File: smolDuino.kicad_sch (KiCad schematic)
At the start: 52 parts, among them J1 Barrel_Jack_Switch, J2 USB_C_Receptacle_USB2.0, J3 2x3 SPI Header, J4 2x5 HV Outputs, J5 I^{2}C Connector, P1 CONN_01X01, P2 CONN_01X01, P3 CONN_01X01, P4 CONN_01X01, P5 Digital, P6 Power, P7 Digital, P8 Analog, Q1 AO3401A, SW1 Enable, SW2 Reset, U1 AP62250smol_A, U2 rp2040smol-c-unit, U3 74AHCT1G04, U4 Charj_smol, U5 AT24CS02-STUM, U6 SN74AHCT125N

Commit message: commit before I ruin too much
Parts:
- added C?: 1uF, Capacitor_SMD:C_0603_1608Metric, symbol Device:C
- added C? (x2): 10uF, Capacitor_SMD:C_0603_1608Metric, symbol Device:C
- added D?: UPS120, MikeFootprintLib:UPS120_D_Powermite_AK, symbol MikeLib:UPS120
- added Q?: AO3401A, Package_TO_SOT_SMD:SOT-23, symbol Transistor_FET:AO3401A
- added R?: 100K, Resistor_SMD:R_0402_1005Metric, symbol Device:R
- added R?: 4.7k, Resistor_SMD:R_0603_1608Metric_Pad0.98x0.95mm_HandSolder, symbol Device:R
- added R?: 1k, Resistor_SMD:R_0402_1005Metric, symbol Device:R
- added U?: LC709203FXE-05MH, MikeFootprintLib:WLCSP9-1.60x1.76mm, symbol MikeLib:LC709203FXE-05MH
- added U?: MCP73831-2-OT, Package_TO_SOT_SMD:SOT-23-5, symbol Battery_Management:MCP73831-2-OT
- P1, P2, P3, P4: now left out of the parts list
- U6: footprint Package_DFN_QFN:Texas_S-PVQFN-N14 -> MikeFootprintLib:74x125_Texas_S-PVQFN-N14
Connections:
- net GND: now also C?.2, C?.2, C?.2, R?.1, U?.2 (VSS), U?.A1 (VSS), U?.B1 (TEST)
- new net: R?.1, U?.1 (STAT)
- new net: R?.2, U?.5 (PROG)
- new net +BATT: C?.1, C?.1, Q?.3 (D), U?.3 (VBAT), U?.A3 (VDD)
- new net SCL: U?.C2 (SCL)
- new net V_{High}Out: D?.1 (K), Q?.2 (S)
- new net V_{USB_Charge}: C?.1, U?.4 (VDD)
- new net V_{USB}: D?.2 (A), Q?.1 (G), R?.2
- new net ~{ChargeEnable}: R?.1
- new net ~{STAT}: R?.2
- no-connect marks 15 -> 18
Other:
- note added: "Charger"
- note added: "Gas Gauge"
- note added: "R2 can be fit with 0 Ohm resistor to allow external charge rate selection"
- note added: "USB -> Battery Backfeed Protection"
- note added: "V_{High} -> 5V if USB connected, else V_{Batt}"

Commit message: Removed the extra stuff i added
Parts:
- removed C?: 1uF, Capacitor_SMD:C_0603_1608Metric, symbol Device:C
- removed C? (x2): 10uF, Capacitor_SMD:C_0603_1608Metric, symbol Device:C
- removed D?: UPS120, MikeFootprintLib:UPS120_D_Powermite_AK, symbol MikeLib:UPS120
- removed Q?: AO3401A, Package_TO_SOT_SMD:SOT-23, symbol Transistor_FET:AO3401A
- removed R?: 100K, Resistor_SMD:R_0402_1005Metric, symbol Device:R
- removed R?: 4.7k, Resistor_SMD:R_0603_1608Metric_Pad0.98x0.95mm_HandSolder, symbol Device:R
- removed R?: 1k, Resistor_SMD:R_0402_1005Metric, symbol Device:R
- removed U?: LC709203FXE-05MH, MikeFootprintLib:WLCSP9-1.60x1.76mm, symbol MikeLib:LC709203FXE-05MH
- removed U?: MCP73831-2-OT, Package_TO_SOT_SMD:SOT-23-5, symbol Battery_Management:MCP73831-2-OT
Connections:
- no-connect marks 18 -> 15
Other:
- note removed: "Charger"
- note removed: "Gas Gauge"
- note removed: "R2 can be fit with 0 Ohm resistor to allow external charge rate selection"
- note removed: "USB -> Battery Backfeed Protection"
- note removed: "V_{High} -> 5V if USB connected, else V_{Batt}"

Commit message: Progress
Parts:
- added C1: 47u, Capacitor_SMD:CP_Elec_6.3x5.4, symbol Device:C_Polarized
- added D3: ChargeEn, LED_SMD:LED_0603_1608Metric, symbol Device:LED
- added R8: 2k, Resistor_SMD:R_0603_1608Metric, symbol Device:R
- C2: renamed from C1; value 10uF -> 4u7
- C3: renamed from C2; value 100nF -> 100n
- C4, C5: value 100nF -> 100n
- J1: value Barrel_Jack_Switch -> DC Barrel Jack
- U1: value AP62250smol_A -> AP62250smol; footprint MikePCBAs:AP62250smol_A -> MikePCBAs:AP62250smol_C
- renumbered ART3 to ART2, ART4 to ART3, ART2 to ART4, C3 to C6, D3 to D4, JP2 to JP1, JP3 to JP2, JP1 to JP3, R6 to R5, R7 to R6, R5 to R7, U6 to U3, U5 to U4, U3 to U5, U4 to U6
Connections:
- net GND: now also C1.2
- net VCC: now also R8.1
- net VIN: now also C1.1
- net ~{ChargeEn}: now reaches U5.4, U6.5 (~{ChargeEnable})
- net ~{ChargeEn}: now also D3.1 (K)
- net STAT: now reaches D4.1 (K), U6.6 (~{STAT})
- net CC2: now reaches J2.B5 (CC2), R4.2
- net V_{Bus}: now reaches F2.1, J2.A4 (VBUS), J2.A9 (VBUS), J2.B4 (VBUS), J2.B9 (VBUS)
- net CC1: now reaches J2.A5 (CC1), R2.2
- net V_{Bus}_{Fused}: now reaches C2.2, C3.1, F2.2, Q1.3 (D)
- new net: D3.2 (A), R8.2
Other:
- moved on the sheet: C4, D4, F1, J1, JP3, U6

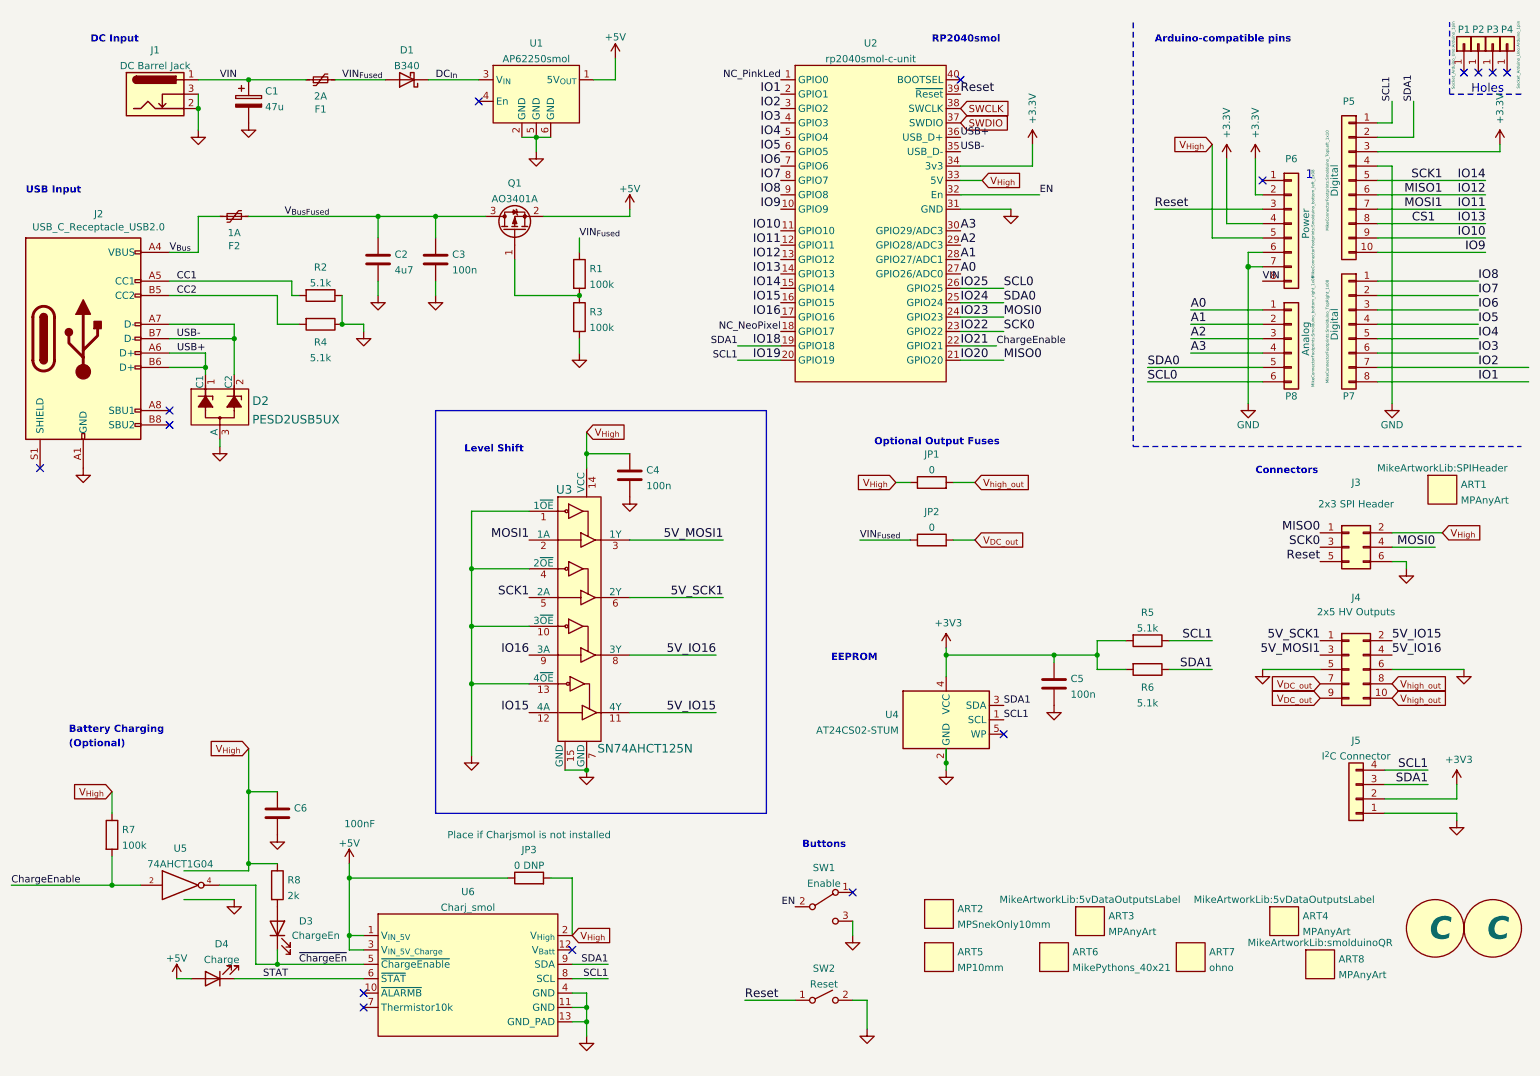
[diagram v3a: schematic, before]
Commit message: More progress. Charjsmol is removed and integrated directly onto the board.
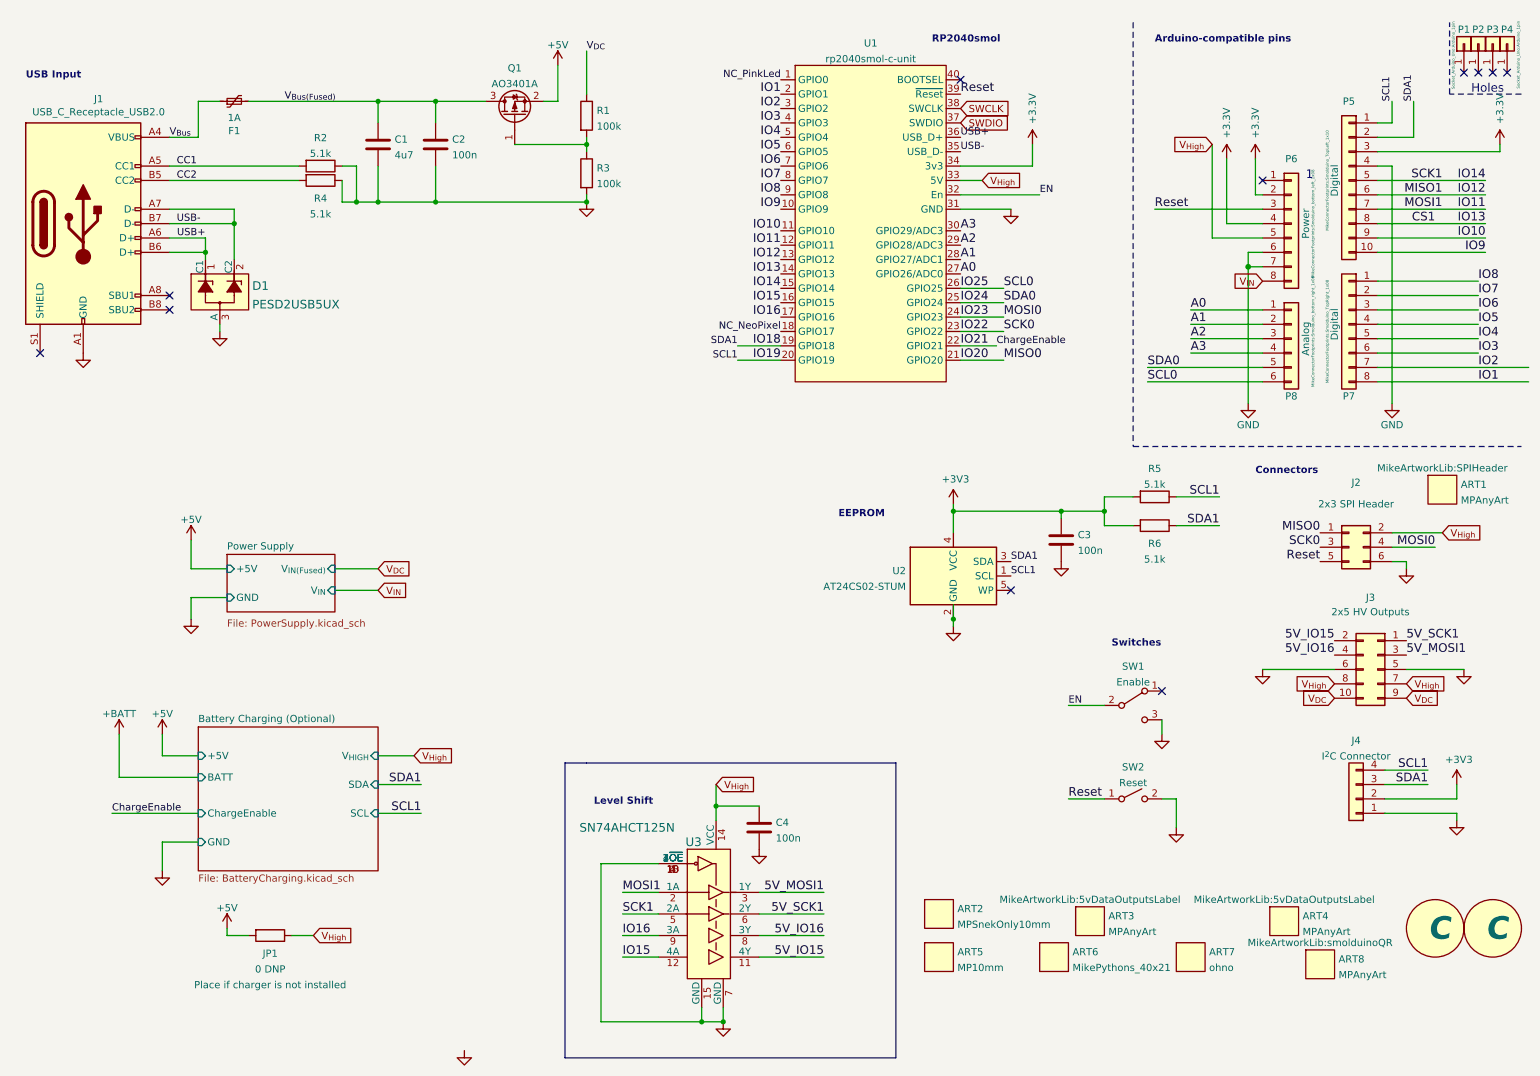
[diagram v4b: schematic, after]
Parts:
- removed C1: 47u, Capacitor_SMD:CP_Elec_6.3x5.4, symbol Device:C_Polarized
- removed C6: 100nF, Capacitor_SMD:C_0603_1608Metric, symbol Device:C
- removed D1: B340, Diode_SMD:D_SMC, symbol Diode:B340
- removed D3: ChargeEn, LED_SMD:LED_0603_1608Metric, symbol Device:LED
- removed D4: Charge, LED_SMD:LED_0603_1608Metric, symbol Device:LED
- removed F1: 2A, Fuse:Fuse_2920_7451Metric, symbol Device:Polyfuse_Small
- removed J1: DC Barrel Jack, Connector_BarrelJack:BarrelJack_GCT_DCJ200-10-A_Horizontal, symbol Connector:Barrel_Jack_Switch
- removed JP2: 0, MikeFootprintLib:R_0OHM_1206_3216Metric, symbol Device:R
- removed JP3: 0 DNP, MikeFootprintLib:R_0OHM_1206_3216Metric, symbol Device:R
- removed R7: 100k, Resistor_SMD:R_0603_1608Metric, symbol Device:R
- removed R8: 2k, Resistor_SMD:R_0603_1608Metric, symbol Device:R
- removed U1: AP62250smol, MikePCBAs:AP62250smol_C, symbol MikeLib:AP62250smol_A
- removed U5: 74AHCT1G04, Package_TO_SOT_SMD:SOT-353_SC-70-5, symbol 74xGxx:74AHCT1G04
- removed U6: Charj_smol, MikePCBAs:Charj_smol_B, symbol MikeLib:Charj_smol
- JP1: value 0 -> 0 DNP; Field4 (none) -> Place if charger is not installed
- U3: footprint MikeFootprintLib:74x125_Texas_S-PVQFN-N14 -> Package_DFN_QFN:Texas_S-PVQFN-N14; symbol MikeLib:SN74AHCT125N -> MikeLib:SN74AHCT125N_OETied
- renumbered C2 to C1, C3 to C2, C5 to C3, D2 to D1, F2 to F1, J2 to J1, J3 to J2, J4 to J3, J5 to J4, U2 to U1, U4 to U2
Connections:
- net +5V: now also JP1.2
- net VCC renamed V_{High}
- net V_{High}: now also J3.7 (Pin_7), J3.8 (Pin_8)
- net VIN renamed V_{IN}
- net VIN_{Fused} renamed V_{DC}
- net V_{DC}: now also J3.10 (Pin_10), J3.9 (Pin_9)
- net V_{Bus}_{Fused} renamed V_{Bus}_{(Fused)}
- removed net V_{DC_out}: J3.7 (Pin_7), J3.9 (Pin_9)
- removed net V_{high_out}: J3.10 (Pin_10), J3.8 (Pin_8), JP1.2
- no-connect marks 15 -> 11
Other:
- added sheet Battery Charging (Optional) (BatteryCharging.kicad_sch)
- added sheet Power Supply (PowerSupply.kicad_sch)
- note added: "Switches"
- note removed: "(Optional)"
- note removed: "Battery Charging"
- note removed: "Buttons"
- note removed: "DC Input"
- note removed: "Optional Output Fuses"
- moved on the sheet: C1, C2, C3, C4, D1, F1, J1, J3, Q1, R1, R2, R3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

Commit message: Rev C, I think
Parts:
- removed ART3, ART4: MPAnyArt, MikeArtworkLib:5vDataOutputsLabel, symbol MikeArtworkLib:MPAnyArt
- added JP1: Jumper_2_Bridged, Jumper:SolderJumper-2_P1.3mm_Bridged_Pad1.0x1.5mm, symbol Jumper:Jumper_2_Bridged
- J3: footprint MikeConnectorFootprints:smolduino_2x05_header -> MikeConnectorFootprints:PinSocket_2x06_P2.54mm_Vertical; symbol Connector_Generic:Conn_02x05_Odd_Even -> Connector_Generic:Conn_02x06_Odd_Even
- JP2: renamed from JP1; value 0 DNP -> Battery Protection Diode Bypass; footprint MikeFootprintLib:R_0OHM_1206_3216Metric -> Jumper:SolderJumper-2_P1.3mm_Open_TrianglePad1.0x1.5mm; symbol Device:R -> Jumper:SolderJumper_2_Open; now left out of the parts list
- renumbered ART5 to ART3, ART6 to ART4, ART7 to ART5, ART8 to ART6
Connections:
- net +5V: now also J3.10 (Pin_10), J3.9 (Pin_9), P6.5 (Pin_5)
- net EN: now also JP1.1 (A); no longer U1.32 (En)
- net V_{DC}: now also J3.11 (Pin_11), J3.12 (Pin_12); no longer J3.10 (Pin_10), J3.9 (Pin_9)
- net V_{High}: no longer P6.5 (Pin_5)
- new net EN_Pin: JP1.2 (B), U1.32 (En)

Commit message: Remove Gas Gauge IC
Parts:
- MISC1, MISC2: value C -> D
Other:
- sheet Battery Charging (Optional) ports: added none; removed SCL, SDA
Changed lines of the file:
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@@
-    (stroke (width 0) (type default) (color 0 0 0 0))
-  )
-  (wire (pts (xy 82.55 147.32) (xy 90.17 147.32))
     (stroke (width 0) (type default) (color 0 0 0 0))
   )
@@
     (stroke (width 0) (type default) (color 0 0 0 0))
   )
-  (wire (pts (xy 82.55 152.4) (xy 90.17 152.4))
-    (stroke (width 0) (type default) (color 0 0 0 0))
-  )
   (wire (pts (xy 223.52 149.86) (xy 223.52 154.94))
     (stroke (width 0) (type default) (color 0 0 0 0))
@@
     (effects (font (size 1.524 1.524)) (justify left bottom))
   )
-  (label "SCL1" (at 90.17 152.4 180)
-    (effects (font (size 1.524 1.524)) (justify right bottom))
-  )
   (label "5V_MOSI1" (at 161.29 166.37 180)
     (effects (font (size 1.524 1.524)) (justify right bottom))
@@
   (label "IO2" (at 276.86 73.66 0)
     (effects (font (size 1.524 1.524)) (justify left bottom))
-  )
-  (label "SDA1" (at 90.17 147.32 180)
-    (effects (font (size 1.524 1.524)) (justify right bottom))
   )
   (label "IO3" (at 276.86 71.12 0)
@@
     (effects (font (size 1.27 1.27)) (justify left))
     (property "Intersheet References" "${INTERSHEET_REFS}" (id 0) (at 269.6937 134.5406 0)
-      (effects (font (size 1.27 1.27)) (justify left) hide)
-    )
-  )
-  (global_label "V_{High}" (shape input) (at 119.38 62.23 0) (fields_autoplaced)
-    (effects (font (size 1.27 1.27)) (justify left))
-    (property "Intersheet References" "${INTERSHEET_REFS}" (id 0) (at 126.2683 62.3094 0)
       (effects (font (size 1.27 1.27)) (justify left) hide)
     )
@@
       (effects (font (size 1.27 1.27)) hide)
     )
-    (property "Value" "C" (id 1) (at 267.97 172.72 0)
+    (property "Value" "D" (id 1) (at 267.97 172.72 0)
       (effects (font (size 4 4) bold italic) (justify left))
     )
@@
       (effects (font (size 1.27 1.27)) hide)
     )
-    (property "Value" "C" (id 1) (at 278.13 172.72 0)
+    (property "Value" "D" (id 1) (at 278.13 172.72 0)
       (effects (font (size 4 4) bold italic) (justify left))
     )
@@
       (effects (font (size 1.27 1.27)) (justify left))
     )
-    (pin "SDA" input (at 82.55 147.32 0)
-      (effects (font (size 1.27 1.27)) (justify right))
-    )
-    (pin "SCL" input (at 82.55 152.4 0)
-      (effects (font (size 1.27 1.27)) (justify right))
-    )
   )
   (sheet (at 55.88 106.68) (size 19.05 10.16)
@@
       (reference "C8") (unit 1) (value "100nF") (footprint "Capacitor_SMD:C_0603_1608Metric")
     )
-    (path "/4df768fb-a916-4507-86ba-485420ee6fae/fcad4bef-02fe-4f0c-bf34-49af1a9bf3a9"
-      (reference "C9") (unit 1) (value "1uF") (footprint "Capacitor_SMD:C_0603_1608Metric")
-    )
     (path "/7f79e8ac-1c7a-4630-a8ac-6a0b87c48f36"
       (reference "D1") (unit 1) (value "PESD2USB5UX") (footprint "digikey-footprints:SOT-23-3")
@@
     )
     (path "/497ffb72-2615-4d8d-ad95-762335aa7838"
-      (reference "MISC1") (unit 1) (value "C") (footprint "MikeFootprintLib:RevisionSymbol")
+      (reference "MISC1") (unit 1) (value "D") (footprint "MikeFootprintLib:RevisionSymbol")
     )
     (path "/4a0bf929-1d2b-4968-bef4-8930fb46e073"
-      (reference "MISC2") (unit 1) (value "C") (footprint "MikeFootprintLib:RevisionSymbol")
+      (reference "MISC2") (unit 1) (value "D") (footprint "MikeFootprintLib:RevisionSymbol")
     )
     (path "/00000000-0000-0000-0000-000056d71177"
@@
       (reference "U6") (unit 1) (value "74AHCT1G04") (footprint "Package_TO_SOT_SMD:SOT-353_SC-70-5")
     )
-    (path "/4df768fb-a916-4507-86ba-485420ee6fae/b010ea46-9a0c-46be-8828-675953280b53"
-      (reference "U7") (unit 1) (value "LC709203FXE-05MH") (footprint "MikeFootprintLib:WLCSP9-1.60x1.76mm")
-    )
-  )
+  )
